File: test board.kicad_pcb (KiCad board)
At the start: 2 copper layers, 138.4 x 111.8 mm, 129 parts, among them J1 Conn_01x02, J10 Conn_01x02, J11 Conn_01x02, J12 Conn_01x02, J13 Conn_01x02, J14 Conn_01x02, J15 Conn_01x02, J16 Conn_01x02, J17 Conn_01x02, J18 Conn_01x02, J19 Conn_01x02, J2 Conn_01x02, J20 Conn_01x02, J21 Conn_01x02, J22 Conn_01x02, J23 Conn_01x07, J24 Conn_01x07, J25 Conn_01x01, J26 Conn_01x01, J3 Conn_01x02, J4 Conn_01x02, J5 Conn_01x02, J6 Conn_01x02, J7 Conn_01x02, J8 Conn_01x02, J9 Conn_01x02, T1 Transformer_1P_1S, T2 Transformer_1P_1S, U1 LM5180QNGURQ1, U2 LM5180QNGURQ1

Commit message: more edits to schematic and began laying out pcb
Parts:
- removed ?: ConstMod5-Vout, TestPoint:TestPoint_Keystone_5005-5009_Compact
- removed ?: ConstMod5-GND, TestPoint:TestPoint_Keystone_5005-5009_Compact
- removed ?: VariableMod2-GND, TestPoint:TestPoint_Keystone_5005-5009_Compact
- removed LOGO3: Logo_Placeholder, UTSVT_Special:Aro
- added TP17: VariableMod2-GND, TestPoint:TestPoint_Keystone_5005-5009_Compact, F.Cu at (105.4, 38.1)
- added TP29: ConstMod5-GND, TestPoint:TestPoint_Keystone_5005-5009_Compact, F.Cu at (160.0, 50.7)
- added TP30: ConstMod5-Vout, TestPoint:TestPoint_Keystone_5005-5009_Compact, F.Cu at (174.0, 50.7)
- C1: value 460u2 -> 460u
- C10: value 500u12 -> 6.8u
- C11: value 22n1 -> 22n
- C12: value 22n2 -> 22n
- C13: value 500u2 -> 500u
- C14: value 500u3 -> 500u
- C15: value 460u1 -> 460u
- C2: value 500u4 -> 6.8u
- C3: value 500u5 -> 6.8u
- C4: value 500u6 -> 6.8u
- C5: value 500u7 -> 6.8u
- C6: value 500u8 -> 6.8u
- C7: value 500u9 -> 6.8u
- C8: value 500u10 -> 6.8u
- C9: value 500u11 -> 6.8u
- LOGO1: value Logo_Placeholder -> Hallock
- LOGO2: value Logo_Placeholder -> UTSVT_Logo
- R1: value 536k1 -> 536k
- R10: value 280ohm4 -> 280
- R11: value 280ohm5 -> 280
- R12: value 280ohm6 -> 280
- R13: value 280ohm7 -> 280
- R14: value 280ohm8 -> 280
- R15: value 280ohm9 -> 280
- R16: value 720ohm1 -> 720
- R17: value 720ohm2 -> 720
- R18: value 720ohm3 -> 720
- R19: value 720ohm4 -> 720
- R2: value 100k1 -> 100k
- R20: value 720ohm5 -> 720
- R21: value 720ohm6 -> 720
- R22: value 720ohm7 -> 720
- R23: value 720ohm8 -> 720
- R24: value 720ohm9 -> 720
- R25: value 1k1 -> 1k
- R26: value 1k2 -> 1k
- R3: value 536k2 -> 536k
- R4: value 100k2 -> 100k
- R5: value 12.1k1 -> 12.1k
- R6: value 12.1k2 -> 12.1k
- R7: value 280ohm1 -> 280
- R8: value 280ohm2 -> 280
- R9: value 280ohm3 -> 280
- gave numbers to parts that had none: 35
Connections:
- C1 pad 1: Net-(C1-Pad1) -> +5V
- C10 pad 2: Net-(C10-Pad2) -> +5V
- C13 pad 2: GNDREF -> Net-(C13-Pad2)
- C14 pad 2: GNDREF -> Net-(C14-Pad2)
- C15 pad 1: Net-(C15-Pad1) -> +5V
- C2 pad 2: Net-(C2-Pad2) -> +5V
- C3 pad 2: Net-(C3-Pad2) -> +5V
- C4 pad 2: Net-(C4-Pad2) -> +5V
- C5 pad 2: Net-(C5-Pad2) -> +5V
- C6 pad 2: Net-(C6-Pad2) -> +5V
- C7 pad 2: Net-(C7-Pad2) -> +5V
- C8 pad 2: Net-(C8-Pad2) -> +5V
- C9 pad 2: Net-(C9-Pad2) -> +5V
- D1 pad 2: Net-(C1-Pad1) -> +5V
- D2 pad 2: Net-(C15-Pad1) -> +5V
- J12 pad 2: GNDREF -> Net-(C14-Pad2)
- J13 pad 2: GNDREF -> Net-(C13-Pad2)
- PS1 pad 2: Net-(C10-Pad2) -> +5V
- PS2 pad 2: Net-(C2-Pad2) -> +5V
- PS3 pad 2: Net-(C3-Pad2) -> +5V
- PS4 pad 2: Net-(C4-Pad2) -> +5V
- PS5 pad 2: Net-(C5-Pad2) -> +5V
- PS6 pad 2: Net-(C6-Pad2) -> +5V
- PS7 pad 2: Net-(C7-Pad2) -> +5V
- PS8 pad 2: Net-(C8-Pad2) -> +5V
- PS9 pad 2: Net-(C9-Pad2) -> +5V
- R1 pad 1: Net-(C15-Pad1) -> +5V
- R3 pad 1: Net-(C1-Pad1) -> +5V
- RV1 pad 1: Net-(D4-Pad2) -> Net-(RV1-Pad1)
- RV2 pad 1: Net-(D3-Pad2) -> Net-(RV2-Pad1)
- T1 pad 1: Net-(C1-Pad1) -> +5V
- T1 pad 3: GNDREF -> Net-(C14-Pad2)
- T2 pad 1: Net-(C15-Pad1) -> +5V
- T2 pad 3: GNDREF -> Net-(C13-Pad2)
- TP19 pad 1: GNDREF -> Net-(C13-Pad2)
- U1 pad 3: Net-(C1-Pad1) -> +5V
- U2 pad 3: Net-(C15-Pad1) -> +5V
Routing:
- net GND: track 320.4 -> 0.00 mm, vias 2 -> 0
- net GNDREF: track 94.6 -> 0.00 mm, vias 1 -> 0
- net Net-(D4-Pad2): track 46.3 -> 0.00 mm
- net Net-(D3-Pad2): track 44.7 -> 0.00 mm
- net Net-(C15-Pad1): track 31.2 -> 0.00 mm, vias 2 -> 0
- net Net-(C1-Pad1): track 28.5 -> 0.00 mm, vias 2 -> 0
- net Net-(J17-Pad2): track 26.5 -> 0.00 mm
- net Net-(J21-Pad2): track 26.3 -> 0.00 mm
- net Net-(J20-Pad2): track 26.3 -> 0.00 mm
- net Net-(J22-Pad2): track 26.3 -> 0.00 mm
- net Net-(J19-Pad2): track 26.3 -> 0.00 mm
- net Net-(J18-Pad2): track 26.3 -> 0.00 mm
- net Net-(J14-Pad2): track 26.1 -> 0.00 mm
- net Net-(J15-Pad2): track 25.4 -> 0.00 mm
- net Net-(J16-Pad2): track 25.2 -> 0.00 mm
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- added copper zone on F.Cu, net +5V
- added copper zone on B.Cu, net GND
- removed copper zone on F.Cu, net (none)
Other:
- board text removed: "const/Var-Mod-Conn"

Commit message: Finished just needs to be double checked
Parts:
- moved D1 0.67 mm to (106.4, 61.3)
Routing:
- net GND: track 0.00 -> 156.0 mm
- net Net-(D4-Pad2): track 0.00 -> 47.8 mm
- net Net-(D3-Pad2): track 0.00 -> 44.2 mm
- net Net-(C14-Pad2): track 0.00 -> 29.3 mm
- net Net-(C13-Pad2): track 0.00 -> 27.7 mm
- net Net-(J14-Pad2): track 0.00 -> 26.5 mm
- net Net-(J20-Pad2): track 0.00 -> 26.3 mm
- net Net-(J17-Pad2): track 0.00 -> 26.3 mm
- net Net-(J19-Pad2): track 0.00 -> 26.3 mm
- net Net-(J18-Pad2): track 0.00 -> 26.3 mm
- net Net-(J21-Pad2): track 0.00 -> 26.2 mm
- net Net-(J22-Pad2): track 0.00 -> 26.2 mm
- net Net-(J15-Pad2): track 0.00 -> 25.3 mm
- net Net-(J16-Pad2): track 0.00 -> 25.0 mm
- net Net-(J14-Pad1): track 0.00 -> 20.6 mm
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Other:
- board text removed: "1"
- board text removed: "10"
- board text removed: "11"
- board text removed: "12"
- board text removed: "13"
- board text removed: "14"
- board text removed: "15"
- board text removed: "16"
- board text removed: "17"
- board text removed: "18"
- board text removed: "19"
- board text removed: "2"
- board text removed: "20"
- board text removed: "21"
- board text removed: "22"
- board text removed: "23"
- board text removed: "24"
- board text removed: "25"
- board text removed: "26"
- board text removed: "27"
- board text removed: "28"
- board text removed: "29"
- board text removed: "3"
- board text removed: "30"
- board text removed: "31"
- board text removed: "32"
- board text removed: "33"
- board text removed: "34"
- board text removed: "35"
- board text removed: "36"
- board text removed: "37"
- board text removed: "38"
- board text removed: "4"
- board text removed: "5"
- board text removed: "6"
- board text removed: "7"
- board text removed: "8"
- board text removed: "9"

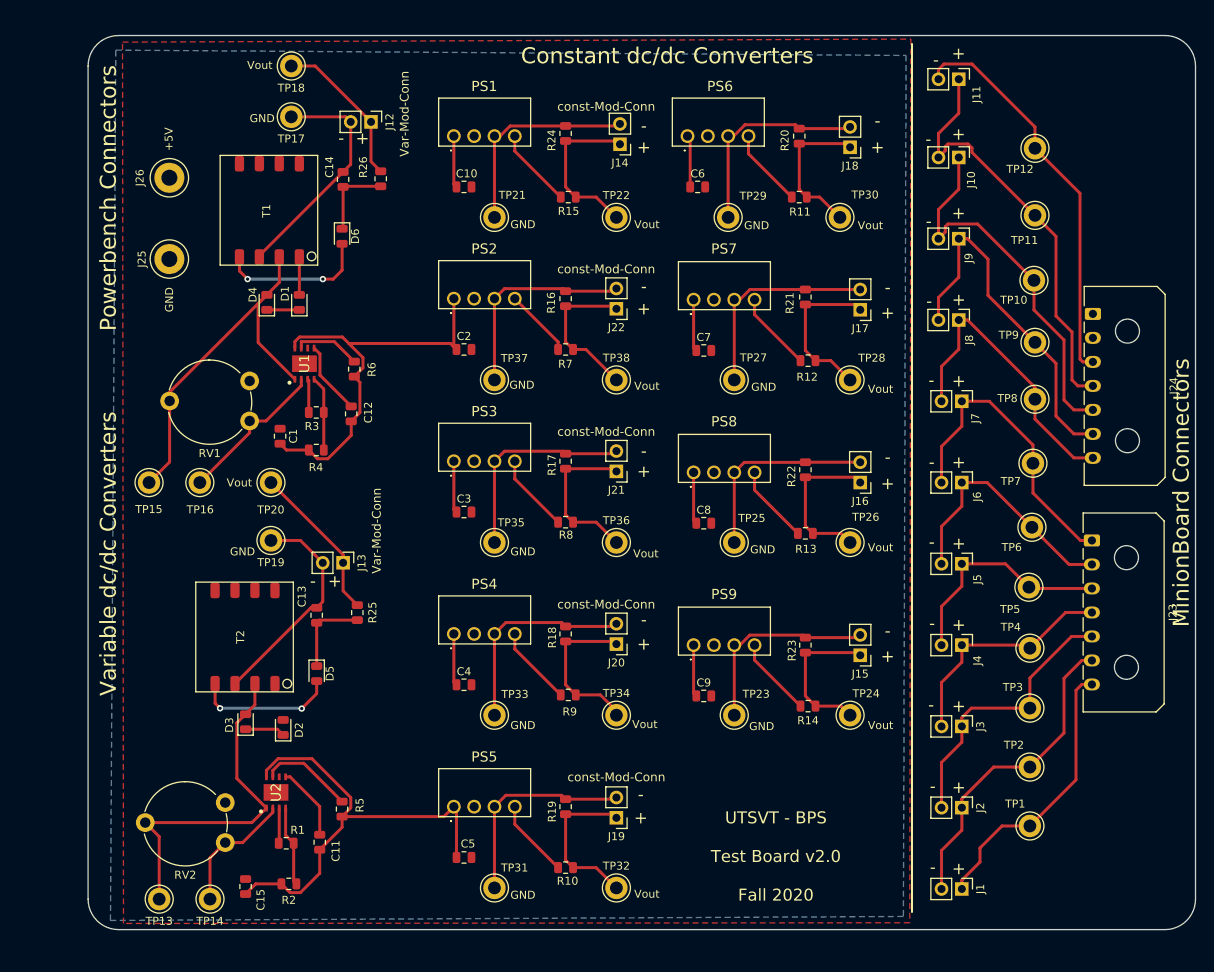
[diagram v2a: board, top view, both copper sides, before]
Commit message: Redoes layout to make the board smaller
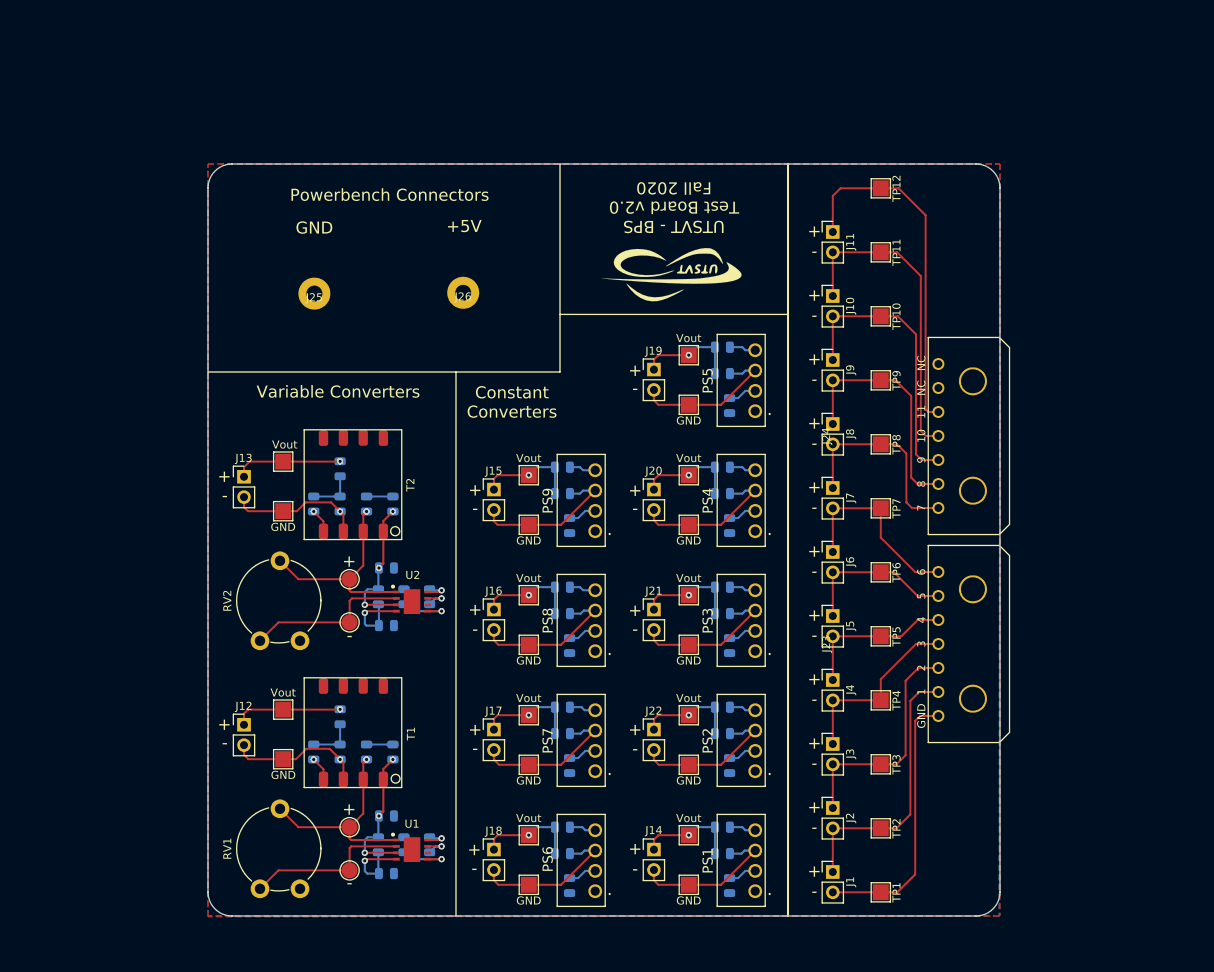
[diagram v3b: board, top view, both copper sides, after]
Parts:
- C1, C10, C11, C12, C13, C14, C15, C2, C3, C4, C5, C6, C7, C8, C9, D1, D2, D3, D4, D5, D6, R1, R10, R11, R12, R13, R14, R15, R16, R17, R18, R19, R2, R20, R21, R22, R23, R24, R25, R26, R3, R4, R5, R6, R7, R8, R9: moved to B.Cu
- J23, J24: footprint Connector_Molex:Molex_Micro-Fit_3.0_43650-0700_1x07_P3.00mm_Horizontal -> UTSVT_Connectors:Molex_MicroFit_01x07_Horizontal
- J25, J26: footprint Connector:Banana_Jack_1Pin -> UTSVT_Connectors:Banana_Jack_1_Pin_4mm
- LOGO2: moved to F.Cu
- TP1, TP10, TP11, TP12, TP17, TP18, TP19, TP2, TP20, TP21, TP22, TP23, TP24, TP25, TP26, TP27, TP28, TP29, TP3, TP30, TP31, TP32, TP33, TP34, TP35, TP36, TP37, TP38, TP4, TP5, TP6, TP7, TP8, TP9: footprint TestPoint:TestPoint_Keystone_5005-5009_Compact -> TestPoint:TestPoint_Pad_2.0x2.0mm
- TP13, TP14, TP15, TP16: footprint TestPoint:TestPoint_Keystone_5005-5009_Compact -> TestPoint:TestPoint_Pad_D2.0mm
- moved PS1 101.6 mm to (163.4, 134.9), turned to 90 degrees
- moved J18 98.4 mm to (130.7, 129.7), turned to 0 degrees
- moved PS6 95.1 mm to (143.4, 134.9), turned to 90 degrees
- moved R20 94.4 mm to (139.3, 130.2), turned to 0 degrees
- moved C10 93.4 mm to (160.2, 134.2), turned to 90 degrees
- moved LOGO2 92.8 mm to (153.2, 57.7)
- moved R24 92.1 mm to (159.3, 130.2), turned to 0 degrees
- moved C6 88.8 mm to (140.2, 134.2), turned to 90 degrees
- moved J14 88.3 mm to (150.7, 129.7), turned to 0 degrees
- moved TP29 87.1 mm to (135.1, 134.1), turned to 180 degrees
- moved TP21 86.9 mm to (155.1, 134.1), turned to 180 degrees
- moved TP30 86.5 mm to (135.1, 127.9), turned to 180 degrees
- moved R11 84.1 mm to (139.3, 126.9), turned to 180 degrees
- moved R15 81.1 mm to (159.3, 126.9), turned to 180 degrees
- moved TP18 80.5 mm to (104.4, 112.2)
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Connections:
- J11 pad 1: Net-(J10-Pad2) -> Net-(J11-Pad1)
- J11 pad 2: Net-(J11-Pad2) -> Net-(J10-Pad1)
- J2 pad 1: Net-(J1-Pad2) -> Net-(J2-Pad1)
- J2 pad 2: Net-(J2-Pad2) -> Net-(J1-Pad1)
- J23 pad 5: Net-(J2-Pad2) -> Net-(J2-Pad1)
- J23 pad 6: Net-(J1-Pad2) -> Net-(J1-Pad1)
- J23 pad 7: Net-(J1-Pad1) -> Net-(J1-Pad2)
- J24 pad 3: Net-(J11-Pad2) -> Net-(J11-Pad1)
- J24 pad 4: Net-(J10-Pad2) -> Net-(J10-Pad1)
- J24 pad 5: Net-(J10-Pad1) -> Net-(J10-Pad2)
- J3 pad 1: Net-(J2-Pad2) -> Net-(J23-Pad4)
- J3 pad 2: Net-(J23-Pad4) -> Net-(J2-Pad1)
- J4 pad 1: Net-(J23-Pad4) -> Net-(J23-Pad3)
- J4 pad 2: Net-(J23-Pad3) -> Net-(J23-Pad4)
- J5 pad 1: Net-(J23-Pad3) -> Net-(J23-Pad2)
- J5 pad 2: Net-(J23-Pad2) -> Net-(J23-Pad3)
- J6 pad 1: Net-(J23-Pad2) -> Net-(J23-Pad1)
- J6 pad 2: Net-(J23-Pad1) -> Net-(J23-Pad2)
- J7 pad 1: Net-(J23-Pad1) -> Net-(J24-Pad7)
- J7 pad 2: Net-(J24-Pad7) -> Net-(J23-Pad1)
- J8 pad 1: Net-(J24-Pad7) -> Net-(J24-Pad6)
- J8 pad 2: Net-(J24-Pad6) -> Net-(J24-Pad7)
- J9 pad 1: Net-(J24-Pad6) -> Net-(J10-Pad2)
- J9 pad 2: Net-(J10-Pad1) -> Net-(J24-Pad6)
- TP1 pad 1: Net-(J1-Pad1) -> Net-(J1-Pad2)
- TP10 pad 1: Net-(J10-Pad1) -> Net-(J10-Pad2)
- TP11 pad 1: Net-(J10-Pad2) -> Net-(J10-Pad1)
- TP12 pad 1: Net-(J11-Pad2) -> Net-(J11-Pad1)
- TP2 pad 1: Net-(J1-Pad2) -> Net-(J1-Pad1)
- TP3 pad 1: Net-(J2-Pad2) -> Net-(J2-Pad1)
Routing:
- net GND: track 156.0 -> 6.78 mm, vias 0 -> 2
- net +5V: track 13.4 -> 67.9 mm, vias 0 -> 6
- net Net-(J11-Pad2): track 49.9 -> 0.00 mm
- net Net-(J11-Pad1): track 0.00 -> 43.9 mm
- net Net-(J2-Pad2): track 35.0 -> 0.00 mm
- net Net-(J2-Pad1): track 0.00 -> 29.1 mm
- net Net-(D4-Pad2): track 47.8 -> 26.3 mm, vias 0 -> 1
- net Net-(J10-Pad2): track 53.3 -> 35.0 mm
- net Net-(D3-Pad2): track 44.2 -> 26.3 mm, vias 0 -> 1
- net Net-(D6-Pad2): track 18.8 -> 2.99 mm, vias 2 -> 1
- net Net-(D5-Pad2): track 17.8 -> 2.99 mm, vias 2 -> 1
- net Net-(J23-Pad1): track 38.2 -> 23.8 mm
- net Net-(J24-Pad6): track 44.6 -> 30.2 mm
- net Net-(J23-Pad2): track 31.7 -> 19.6 mm
- net Net-(C14-Pad2): track 29.3 -> 17.4 mm, vias 0 -> 1
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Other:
- board size 138.4 x 111.8 mm -> 99 x 94 mm
- board text added: "1"
- board text added: "10"
- board text added: "11"
- board text added: "2"
- board text added: "3"
- board text added: "4"
- board text added: "5"
- board text added: "6"
- board text added: "7"
- board text added: "8"
- board text added: "9"
- board text added: "Constant Converters"
- board text added: "Dr. Gary Hallock"
- board text added: "NC"
- board text added: "Variable Converters"
- board text removed: "Constant dc/dc Converters"
- board text removed: "Dr.Hallock"
- board text removed: "MinionBoard Connectors"
- board text removed: "Var-Mod-Conn"
- board text removed: "Variable dc/dc Converters"
- board text removed: "const-Mod-Conn"
